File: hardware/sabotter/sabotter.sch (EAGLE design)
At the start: 112 parts, among them IC1 MAX3232CSE, IC2 MAX3232CSE, IC3 OKI-78SR-3.3/1.5-W36H-C, IC4 OKI-78SR-5/1.5-W36H-C, IC6 ATXMEGA256A3U-AU, IC7 LM4871M, T1 2n2222, T2 2n2222, T3 2n2222

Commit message: radiospares part number added
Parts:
- C13: value 10UFC -> 10µF 35V; device robotter_capacitor:10UFC -> robotter_capacitor:10UF-C_35V
- C14, C15, C16, C2: value 10UFC -> 10UF-C_25V; device robotter_capacitor:10UFC -> robotter_capacitor:10UF-C_25V
- C27, C29: device robotter_capacitor:C_1UF -> robotter_capacitor:1UFD_25V
- C28, C30, C32: value C_10UF -> 10UF-C_25V; device robotter_capacitor:C_10UF -> robotter_capacitor:10UF-C_25V
- C31: value 100NF_50V_0805 -> 100nF_0603_50V; device robotter_capacitor:C_100NF -> robotter_capacitor:100NF-F
- D1: device diode:MBRA340T3 -> robotter_diode:MBRA340T3
- USB: device con-hirose:MINI-USB-SHIELD-UX60-MB-5S8 -> robotter_connector:MINI-USB-SHIELD-UX60-MB-5S8
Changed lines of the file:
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@@
 <?xml version="1.0" encoding="utf-8"?>
 <!DOCTYPE eagle SYSTEM "eagle.dtd">
-<eagle version="6.4">
+<eagle version="6.5.0">
 <drawing>
 <settings>
@@
 <part name="SD1" library="robotter_connector" deviceset="49225-0821" device=""/>
 <part name="C1" library="robotter_capacitor" deviceset="100NF" device="-F" value="100nF_0603_50V"/>
-<part name="C2" library="robotter_capacitor" deviceset="10UF" device="C"/>
+<part name="C2" library="robotter_capacitor" deviceset="10UF" device="-C_25V"/>
 <part name="+3V1" library="supply1" deviceset="+3V3" device=""/>
 <part name="+3V2" library="supply1" deviceset="+3V3" device=""/>
@@
 <part name="UART_C0" library="robotter_connector" deviceset="COM_2013_MASTER" device=""/>
 <part name="GND17" library="supply1" deviceset="GND" device=""/>
-<part name="USB" library="con-hirose" deviceset="MINI-USB-SHIELD-" device="UX60-MB-5S8" value="UX60SC-MB-5S8"/>
+<part name="USB" library="robotter_connector" deviceset="MINI-USB-SHIELD-" device="UX60-MB-5S8" value="UX60SC-MB-5S8"/>
 <part name="GND18" library="supply1" deviceset="GND" device=""/>
 <part name="IC3" library="robotter_ic" deviceset="OKI-78SR" device="-3.3/1.5-W36H-C"/>
@@
 <part name="GND22" library="supply1" deviceset="GND" device=""/>
 <part name="P+4" library="supply1" deviceset="+12V" device=""/>
-<part name="C13" library="robotter_capacitor" deviceset="10UF" device="C"/>
-<part name="C14" library="robotter_capacitor" deviceset="10UF" device="C"/>
-<part name="C15" library="robotter_capacitor" deviceset="10UF" device="C"/>
+<part name="C13" library="robotter_capacitor" deviceset="10UF" device="-C_35V" value="10µF 35V"/>
+<part name="C14" library="robotter_capacitor" deviceset="10UF" device="-C_25V"/>
+<part name="C15" library="robotter_capacitor" deviceset="10UF" device="-C_25V"/>
 <part name="XB1" library="maxstream" deviceset="XBEE" device="-PRO"/>
-<part name="C16" library="robotter_capacitor" deviceset="10UF" device="C"/>
+<part name="C16" library="robotter_capacitor" deviceset="10UF" device="-C_25V"/>
 <part name="C17" library="robotter_capacitor" deviceset="100NF" device="-F" value="100nF_0603_50V"/>
 <part name="+3V7" library="supply1" deviceset="+3V3" device=""/>
 <part name="GND23" library="supply1" deviceset="GND" device=""/>
 <part name="GND24" library="supply1" deviceset="GND" device=""/>
-<part name="D1" library="diode" deviceset="MBRA340T3" device=""/>
+<part name="D1" library="robotter_diode" deviceset="MBRA340T3" device=""/>
 <part name="T1" library="transistor-neu-to92" deviceset="*-NPN-" device="SOT23-BEC" technology="MMBT2222ALT1" value="2n2222"/>
 <part name="T2" library="transistor-neu-to92" deviceset="*-NPN-" device="SOT23-BEC" technology="MMBT2222ALT1" value="2n2222"/>
@@
 <part name="R37" library="robotter_resistor" deviceset="10K" device="-F"/>
 <part name="IC7" library="robotter_ic" deviceset="LM4871" device="M"/>
-<part name="C27" library="robotter_capacitor" deviceset="C_" device="1UF" value="1UF_50V_1206"/>
-<part name="C28" library="robotter_capacitor" deviceset="C_" device="10UF"/>
-<part name="C29" library="robotter_capacitor" deviceset="C_" device="1UF" value="1UF_50V_1206"/>
+<part name="C27" library="robotter_capacitor" deviceset="1UF" device="D_25V" value="1UF_50V_1206"/>
+<part name="C28" library="robotter_capacitor" deviceset="10UF" device="-C_25V"/>
+<part name="C29" library="robotter_capacitor" deviceset="1UF" device="D_25V" value="1UF_50V_1206"/>
 <part name="P+6" library="supply1" deviceset="+5V" device=""/>
 <part name="GND28" library="supply1" deviceset="GND" device=""/>
 <part name="GND29" library="supply1" deviceset="GND" device=""/>
 <part name="GND30" library="supply1" deviceset="GND" device=""/>
-<part name="C30" library="robotter_capacitor" deviceset="C_" device="10UF"/>
-<part name="C31" library="robotter_capacitor" deviceset="C_" device="100NF" value="100NF_50V_0805"/>
+<part name="C30" library="robotter_capacitor" deviceset="10UF" device="-C_25V"/>
+<part name="C31" library="robotter_capacitor" deviceset="100NF" device="-F" value="100nF_0603_50V"/>
 <part name="R38" library="robotter_resistor" deviceset="10K" device="-F"/>
 <part name="R39" library="robotter_resistor" deviceset="10K" device="-F"/>
@@
 <part name="GND31" library="supply1" deviceset="GND" device=""/>
 <part name="GND32" library="supply1" deviceset="GND" device=""/>
-<part name="C32" library="robotter_capacitor" deviceset="C_" device="10UF"/>
+<part name="C32" library="robotter_capacitor" deviceset="10UF" device="-C_25V"/>
 </parts>
 <sheets>
@@
 </segment>
 <segment>
-<pinref part="R1" gate="G$1" pin="1"/>
-<pinref part="R1" gate="G$1" pin="1"/>
 <pinref part="GND3" gate="1" pin="GND"/>
-<wire x1="83.82" y1="-279.4" x2="83.82" y2="-281.94" width="0.1524" layer="91"/>
 <pinref part="R34" gate="G$1" pin="1"/>
 <wire x1="93.98" y1="-279.4" x2="93.98" y2="-281.94" width="0.1524" layer="91"/>
 <wire x1="93.98" y1="-281.94" x2="83.82" y2="-281.94" width="0.1524" layer="91"/>
+<pinref part="R1" gate="G$1" pin="1"/>
+<pinref part="R1" gate="G$1" pin="1"/>
+<wire x1="83.82" y1="-279.4" x2="83.82" y2="-281.94" width="0.1524" layer="91"/>
 <junction x="83.82" y="-281.94"/>
 </segment>

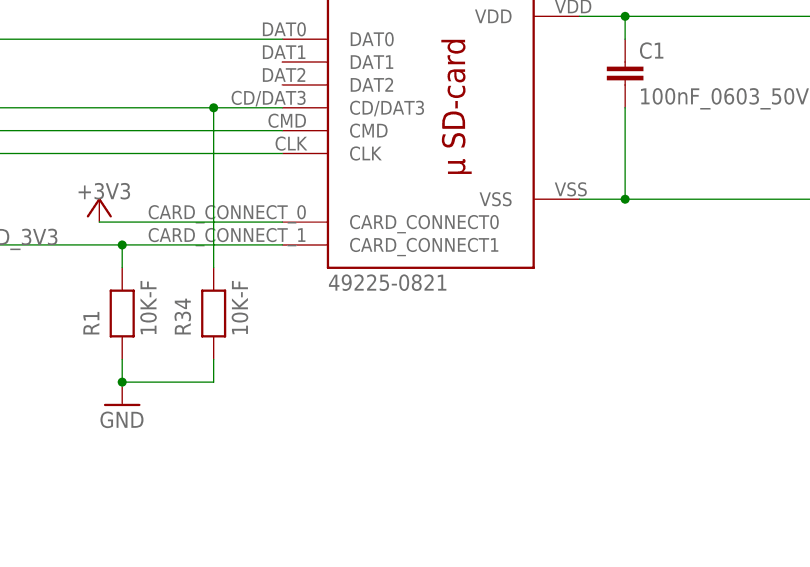
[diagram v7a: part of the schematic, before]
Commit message: footprint correction
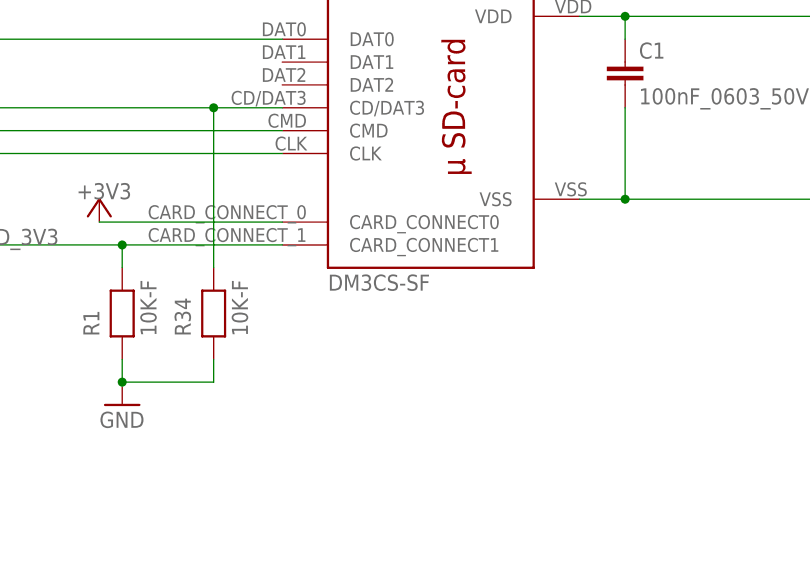
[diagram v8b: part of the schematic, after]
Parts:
- SD1: value 49225-0821 -> DM3CS-SF; device robotter_connector:49225-0821 -> robotter_connector:DM3CS-SF
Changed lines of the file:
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@@
 <part name="FRAME5" library="frames" deviceset="A4L-LOC" device=""/>
 <part name="FRAME6" library="frames" deviceset="A4L-LOC" device=""/>
-<part name="SD1" library="robotter_connector" deviceset="49225-0821" device=""/>
+<part name="SD1" library="robotter_connector" deviceset="DM3CS-SF" device=""/>
 <part name="C1" library="robotter_capacitor" deviceset="100NF" device="-F" value="100nF_0603_50V"/>
 <part name="C2" library="robotter_capacitor" deviceset="10UF" device="-C_25V"/>
